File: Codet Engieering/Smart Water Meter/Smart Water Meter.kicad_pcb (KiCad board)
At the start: 2 copper layers, 60 x 60 mm, 30 parts, among them J1 Barrel_Jack_Switch, J2 Screw_Terminal_01x02, J3 Conn_01x12_Pin, J4 Conn_01x07_Pin, J5 Conn_01x08_Pin, J6 Screw_Terminal_01x03, J7 Screw_Terminal_01x02, K1 SRD-05VDC-SL-C, Q1 BC547, U1 L7805CV

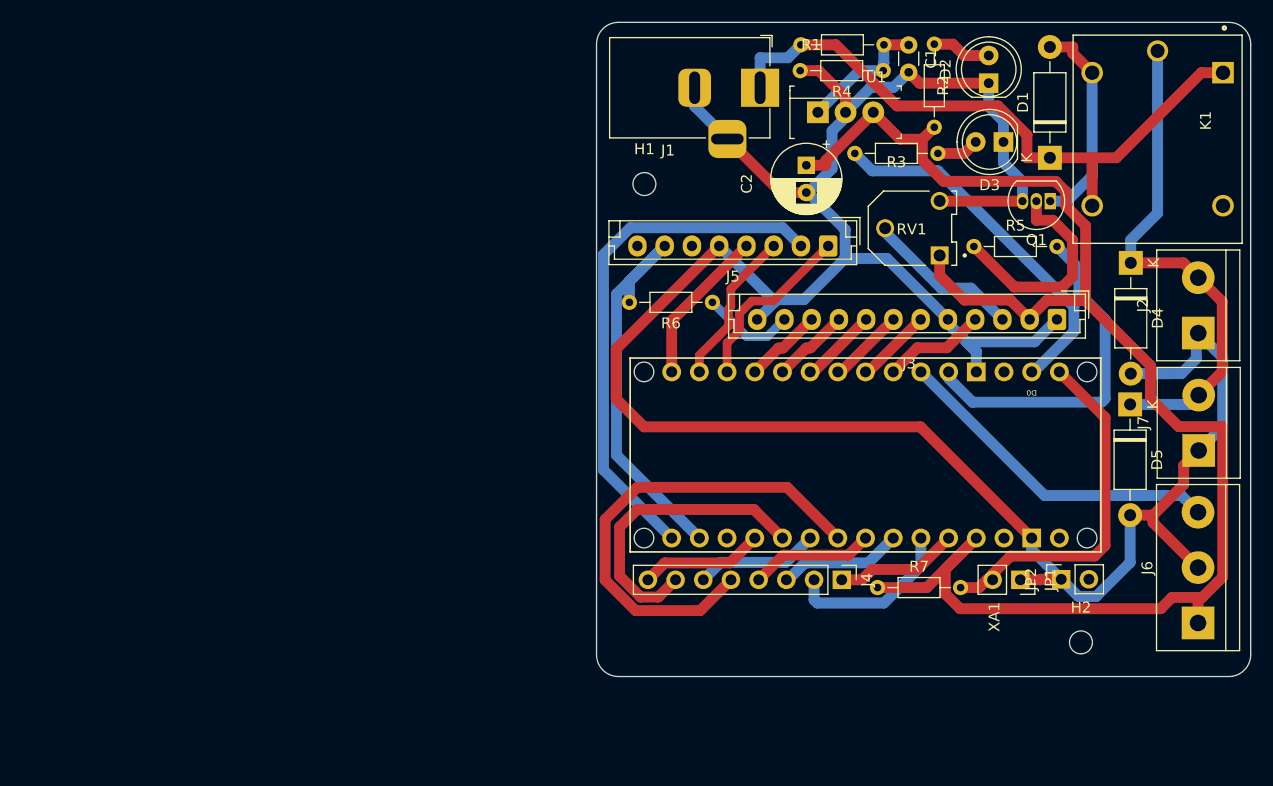
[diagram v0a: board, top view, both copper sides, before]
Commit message: Redessigned the board to fit into asingle layer pcb for local production
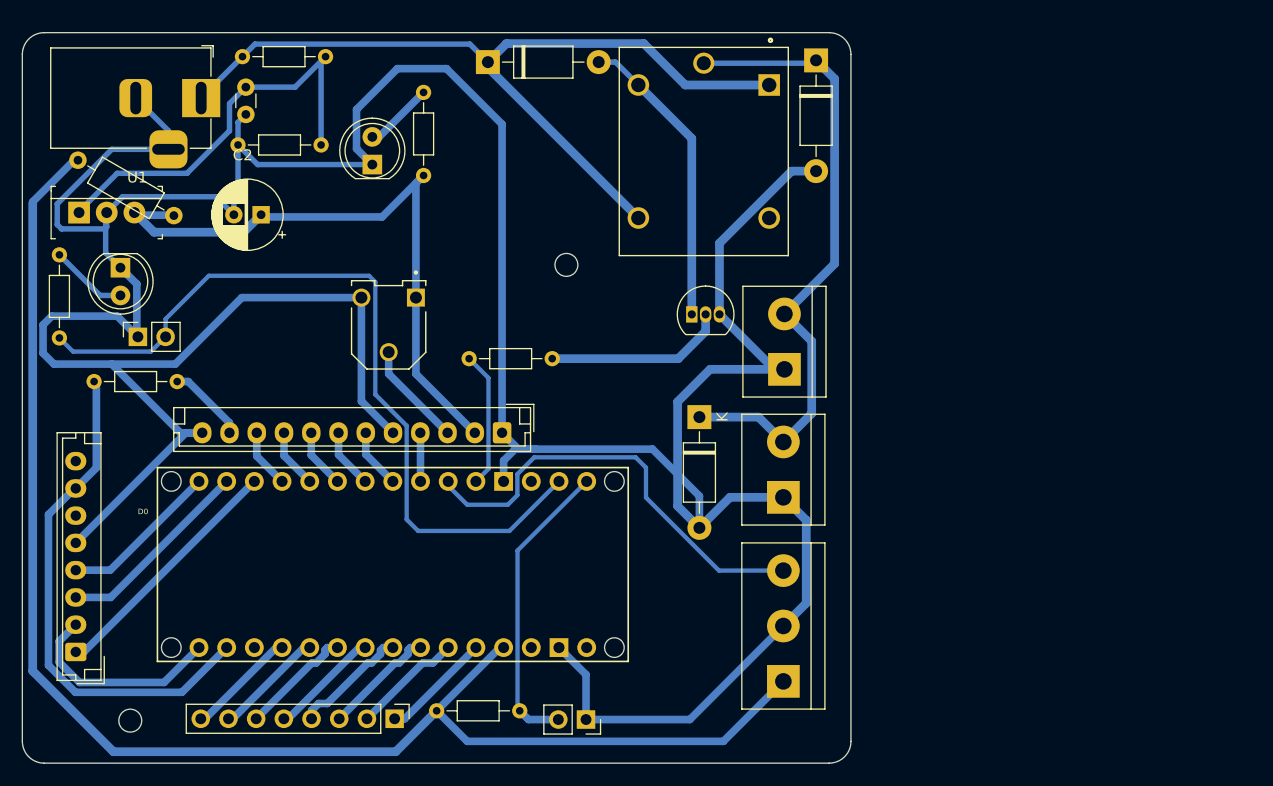
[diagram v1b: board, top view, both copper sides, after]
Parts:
- added Jumper: 220R, Resistor_THT:R_Axial_DIN0207_L6.3mm_D2.5mm_P10.16mm_Horizontal, F.Cu at (105.4, 66.6)
- R3: value 1K -> 220R
- moved JP2 87.6 mm to (110.9, 82.8)
- moved D3 81.8 mm to (109.3, 76.5), turned to -90 degrees
- moved J5 78.4 mm to (105.2, 111.7), turned to 90 degrees
- moved R3 74.9 mm to (103.7, 82.9), turned to 90 degrees
- moved U1 68.4 mm to (105.5, 71.4)
- moved H1 68.2 mm to (110.2, 118.0)
- moved C1 60.9 mm to (120.8, 59.9)
- moved H2 58.5 mm to (150.2, 76.2)
- moved D2 57.0 mm to (132.4, 67.0)
- moved D1 52.3 mm to (143.0, 57.6), turned to 0 degrees
- moved R4 52.0 mm to (127.7, 65.2)
- moved J3 51.9 mm to (144.3, 91.6)
- moved J1 51.3 mm to (116.7, 60.9)
- moved R1 51.2 mm to (120.5, 57.1)
- moved C2 50.2 mm to (122.2, 71.6), turned to 180 degrees
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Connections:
- J5 pad 6: RST -> unconnected-(J5-Pin_6-Pad6)
- R3 pad 1: Net-(XA1-D0/RX) -> Buzzer
- XA1 pad D0: Net-(XA1-D0/RX) -> Buzzer
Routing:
- net GND: track 240.9 -> 340.4 mm
- net Buzzer: track 0.00 -> 72.8 mm
- net 5V: track 139.9 -> 193.7 mm
- net Net-(J4-Pin_5): track 43.9 -> 10.2 mm
- net Net-(XA1-D0/RX): track 33.6 -> 0.00 mm
- net Net-(J5-Pin_2): track 48.4 -> 19.0 mm
- net Net-(U1-IN): track 12.3 -> 38.3 mm
- net PUMP CONTROL: track 31.8 -> 12.5 mm
- net 12V: track 58.9 -> 77.1 mm
- net Net-(J4-Pin_7): track 27.8 -> 10.2 mm
- net Net-(D4-K): track 46.4 -> 58.8 mm
- net SIGNAL: track 30.7 -> 40.7 mm
- net Net-(J5-Pin_7): track 38.3 -> 47.1 mm
- net Net-(D1-A): track 19.5 -> 27.6 mm
- net Net-(J5-Pin_1): track 16.5 -> 22.9 mm
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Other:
- board size 60 x 60 mm -> 76 x 67 mm
